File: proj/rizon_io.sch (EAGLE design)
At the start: 13 parts, among them U1 PC16550DPLCC, U11 74138PDIP, U3 MAX232NPDIP, U7 7805TO220, X1 18.432Mhz

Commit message: Further designed Rizon I/O module schematic
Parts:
- added J1: DB9A-DS09AKG, dooba:DB9A-DS09AKG
- added U2: 7432PDIP, dooba:7432PDIP
- added U4: 7400PDIP, dooba:7400PDIP
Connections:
- new net INT_UART: U2.1Y, U4.2A, U4.2B
- new net INT_UART1: U2.1B
- new net N$2: U4.2Y
- new net RESET: U1.MR, U4.1Y
- net !RESET: now also U4.1A, U4.1B
- net GND: now also U2.GND, U4.GND
- net INT_UART0: now also U2.1A
- net VCC_IO: now also U2.VCC, U4.VCC
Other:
- note added: "I/O Board Power Supply"
- note added: "Rizon computer"
- note added: "Serial Port 0"
- note added: "UART Clock Source"
- moved on the sheet: C1, C2, C3, C4, C5, C6, C7, U1, U3, U7, X1, Z1

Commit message: Routed Rizon I/O board
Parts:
- added C10, C11, C12, C13, C8, C9: 1uF, dooba:CAP508
- added C14: 100nF, dooba:CAPDISC
- added P1: UART1(GND-TX-RX), dooba:PIN_3
- added P2: SCR0, dooba:PIN_8
- added P3: !IODEV[3..7], dooba:PIN_5
- added P4: VIN, dooba:PIN_2
- added P5: VCC_IO, dooba:PIN_2
- added U10: 74273PDIP, dooba:74273PDIP
- added U5, U6: 74590PDIP, dooba:74590PDIP
- added U8: PC16550DPLCC, dooba:PC16550DPLCC
- C7: value CAPDISC -> 100nF
- U7: value 7805TO220 -> 7805TO220H; device dooba:7805TO220 -> dooba:7805TO220H
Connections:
- new net !SCR0_CP: U2.3Y, U4.3A, U4.3B
- new net !TIMER_CLR: P2.3, U10.Q2, U5.!CCLR, U6.!CCLR
- new net CLK_UART1_RX: U8.!BAUDOUT, U8.RCLK
- new net INT_DEV: U2.2Y, U4.2A
- new net INT_EN: P2.2, U10.Q1, U4.2B
- new net INT_TIMER: U2.2B
- new net N$1: U5.!RCO, U6.!CCKEN
- new net N$10: P2.8, U10.Q7
- new net N$11: P2.7, U10.Q6
- new net N$3: C11.1, U3.C2-
- new net N$4: C9.1, U3.C1-
- new net N$5: C9.2, U3.C1+
- new net N$6: C10.1, U3.VS+
- new net N$7: C12.2, U3.VS-
- new net N$8: J1.TXD, U3.T1OUT
- new net N$9: J1.RXD, U3.R1IN
- new net SCR0_CP: U10.CP, U4.3Y
- new net TIMER_OUT: U6.Q7
- new net UART1_RX: P1.3, U8.SIN
- new net UART1_TX: P1.2, U8.SOUT
- net !INT: now also U4.2Y
- net !IODEV0: now also U2.3A
- net !IODEV1: now also U1.!CS2
- net !IODEV2: now also U8.!CS2
- net !IODEV3: now also P3.1
- net !IODEV4: now also P3.2
- net !IODEV5: now also P3.3
- net !IODEV6: now also P3.4
- net !IODEV7: now also P3.5
- net !RD: now also U8.!RD
- net !RESET: now also U10.!MR
- net !ROM_EN: now also P2.1, U10.Q0
- net !WR: now also U2.3B, U8.!WR
- net ADDR0: now also U8.A0
- net ADDR1: now also U8.A1
- net ADDR2: now also U8.A2
- net CLK: now also U5.CCLK, U5.RCLK, U6.CCLK, U6.RCLK
- net CLK_UART: now also U8.XIN
- net DATA0: now also U10.D0, U8.D0
- net DATA1: now also U10.D1, U8.D1
- net DATA2: now also U10.D2, U8.D2
- net DATA3: now also U10.D3, U8.D3
- net DATA4: now also U10.D4, U8.D4
- net DATA5: now also U10.D5, U8.D5
- net DATA6: now also U10.D6, U8.D6
- net DATA7: now also U10.D7, U8.D7
- net GND: now also C12.1, C13.1, C14.1, C8.1, J1.GND, P1.1, P4.2, P5.2, U10.GND, U3.GND, U5.!CCKEN, U5.!OE, U5.GND, U6.!OE, U6.GND, U8.!ADS, U8.GND, U8.RD, U8.WR
- net INT_UART: now also U2.2A; no longer U4.2A, U4.2B
- net INT_UART1: now also U8.INTR
- net N$12: now also P2.6, U10.Q5; no longer U1.CS0
- net N$13: now also P2.5, U10.Q4; no longer U1.CS1
- net N$14: now also P2.4, U10.Q3; no longer U1.!CS2
- net N$2: now also C11.2, U3.C2+; no longer U4.2Y
- net RESET: now also U8.MR
- net UART0_RX: now also U3.R1OUT
- net UART0_TX: now also U3.T1IN
- net VCC_IO: now also C10.2, C13.2, C14.2, C8.2, P5.1, U1.CS0, U1.CS1, U10.VCC, U3.VCC, U5.VCC, U6.VCC, U8.CS0, U8.CS1, U8.VCC
- net VIN: now also P4.1
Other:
- note added: "Glue Logic"
- note added: "Interrupt Logic"
- note added: "SCR0 - System Control Register 0"
- note added: "Serial Port 1"
- note added: "System Timer"
- moved on the sheet: C6, C7, J1, U1, U11, U3, Z1

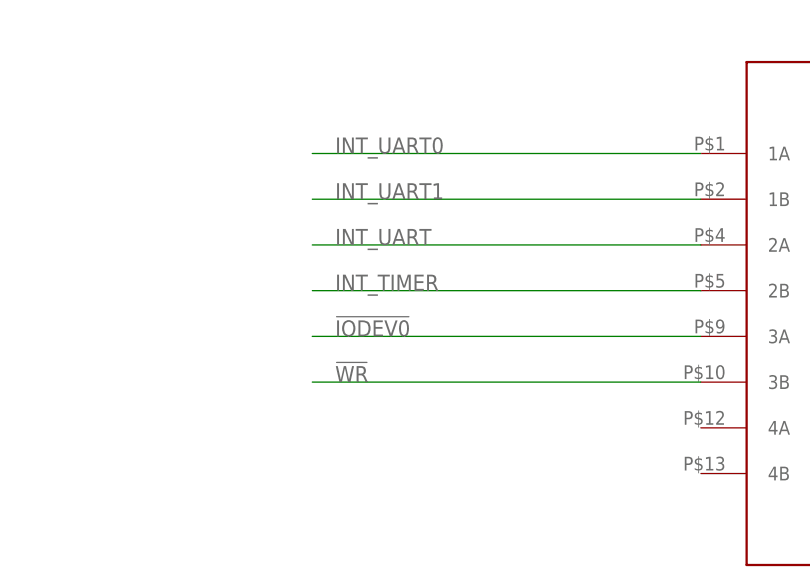
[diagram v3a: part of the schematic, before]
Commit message: Added missing signal net (TIMER_OUT -> INT_TIMER) in Rizon I/O board Further routed SMD version of Rizon computer
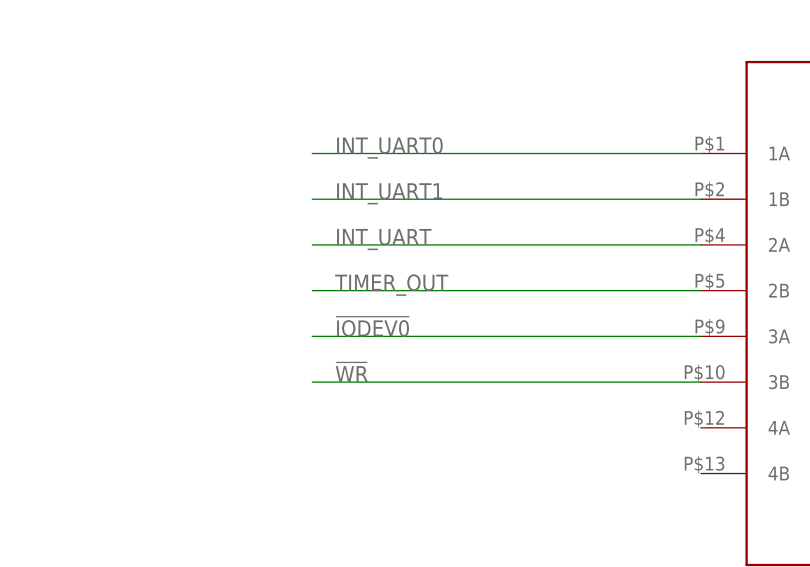
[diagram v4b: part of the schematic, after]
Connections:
- removed net INT_TIMER: U2.2B
- net TIMER_OUT: now also U2.2B
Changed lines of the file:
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@@
 <label x="487.68" y="-106.68" size="1.778" layer="95"/>
 </segment>
-</net>
-<net name="INT_TIMER" class="0">
 <segment>
 <pinref part="U2" gate="U1" pin="2B"/>
